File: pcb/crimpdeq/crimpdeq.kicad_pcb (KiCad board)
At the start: 4 copper layers, 30 x 30 mm, 55 parts, among them J10 A-_Cable_Pad, J11 E+_Cable_Pad, J12 E-_Cable_Pad, J2 USB4105-GF-A, J5 B-_Cable_Pad, J6 SW+_Cable_Pad, J7 B+_Cable_Pad, J8 SW-_Cable_Pad, J9 A+_Cable_Pad, Q2 DMG3415U, U1 ESP32-C3-MINI-1, U2 MCP73831T-2ACI/OT, U3 ADS1220, U5 MAX17048G+T10, U6 SY8088

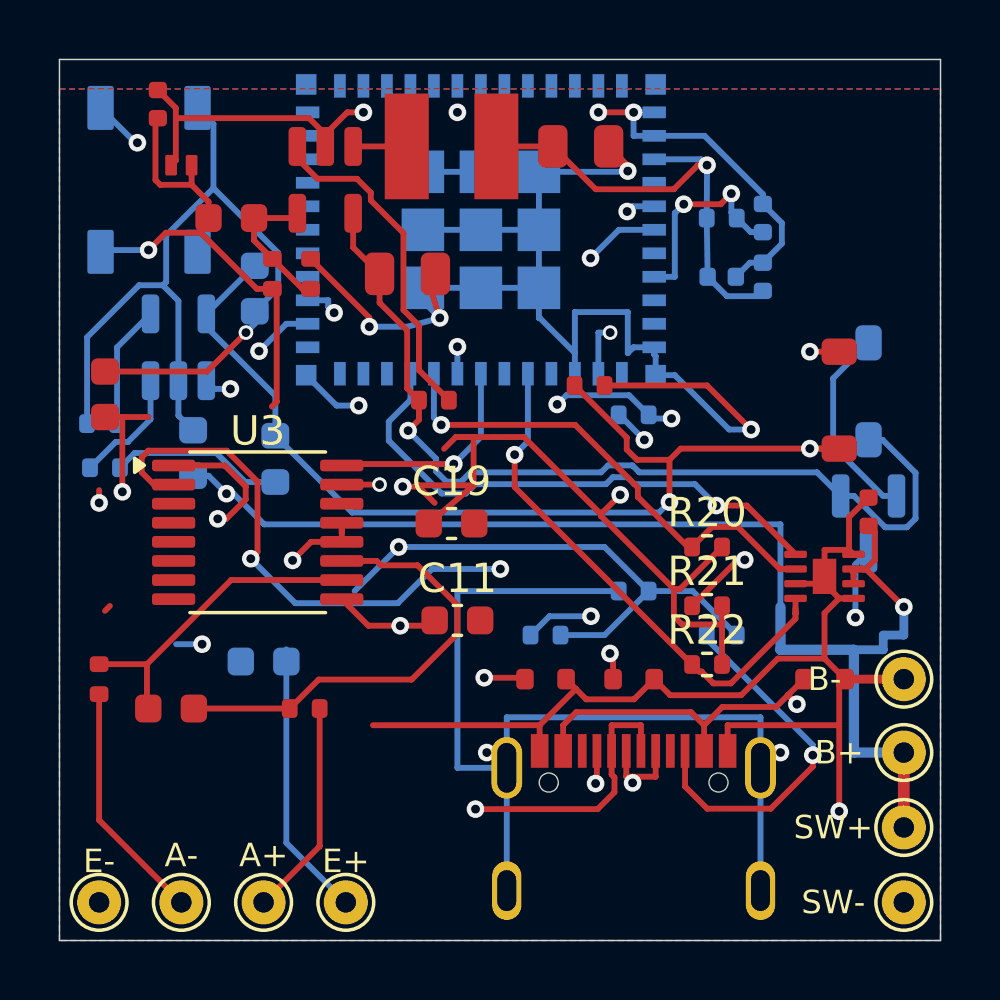
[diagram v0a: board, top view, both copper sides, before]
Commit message: fix: correct SY8088 footprint handedness
Co-authored-by: Cursor <cursoragent@cursor.com>
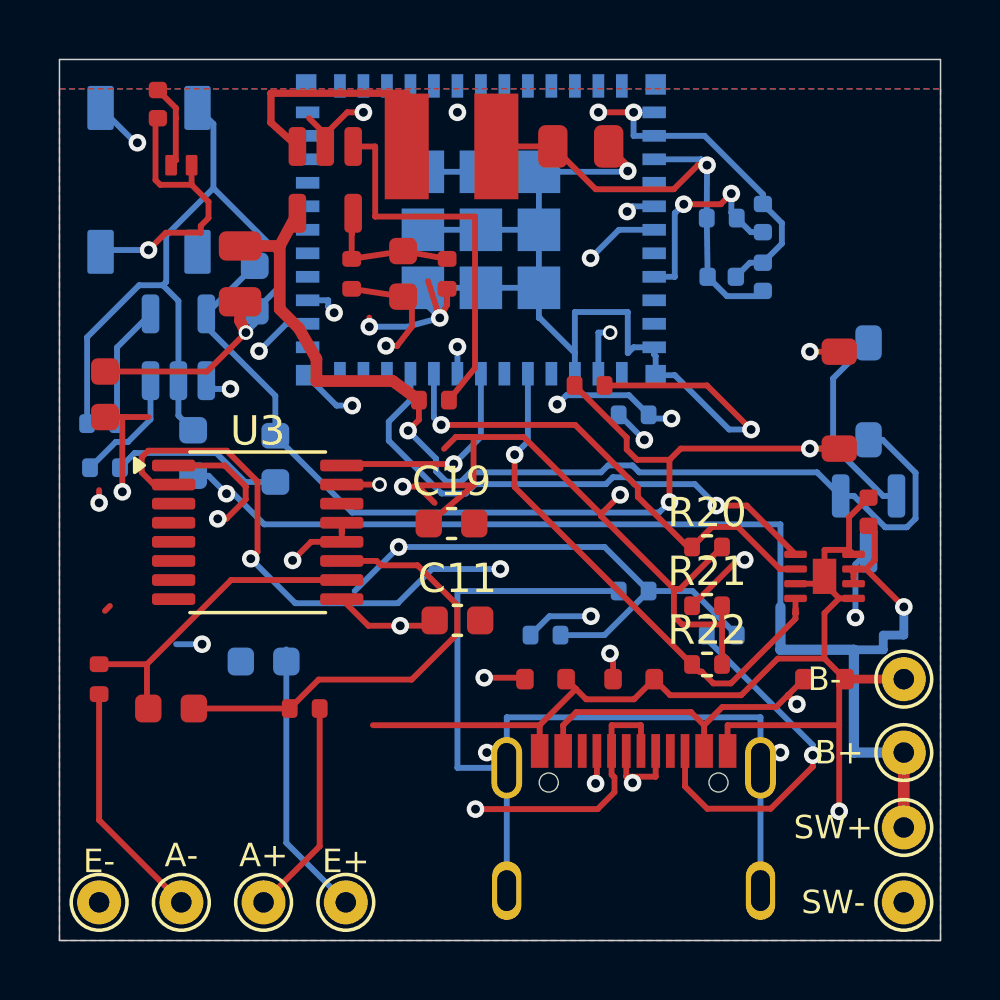
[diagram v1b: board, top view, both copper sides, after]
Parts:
- moved C16 6.15 mm to (139.2, 59.7), turned to 90 degrees
- moved C15 5.70 mm to (133.6, 59.7), turned to -90 degrees
- moved R16 4.65 mm to (140.7, 59.7), turned to -90 degrees
- moved R15 2.70 mm to (137.4, 59.7)
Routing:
- net GND: track 190.4 -> 176.4 mm
- net Buck_Coil: track 1.83 -> 6.84 mm
- net +3V3: track 123.8 -> 127.9 mm, vias 8 -> 9
- net VSYS: track 31.6 -> 35.6 mm
- net ENABLE: track 11.6 -> 13.1 mm

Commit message: fix: correct component footprint handedness
Co-authored-by: Cursor <cursoragent@cursor.com>
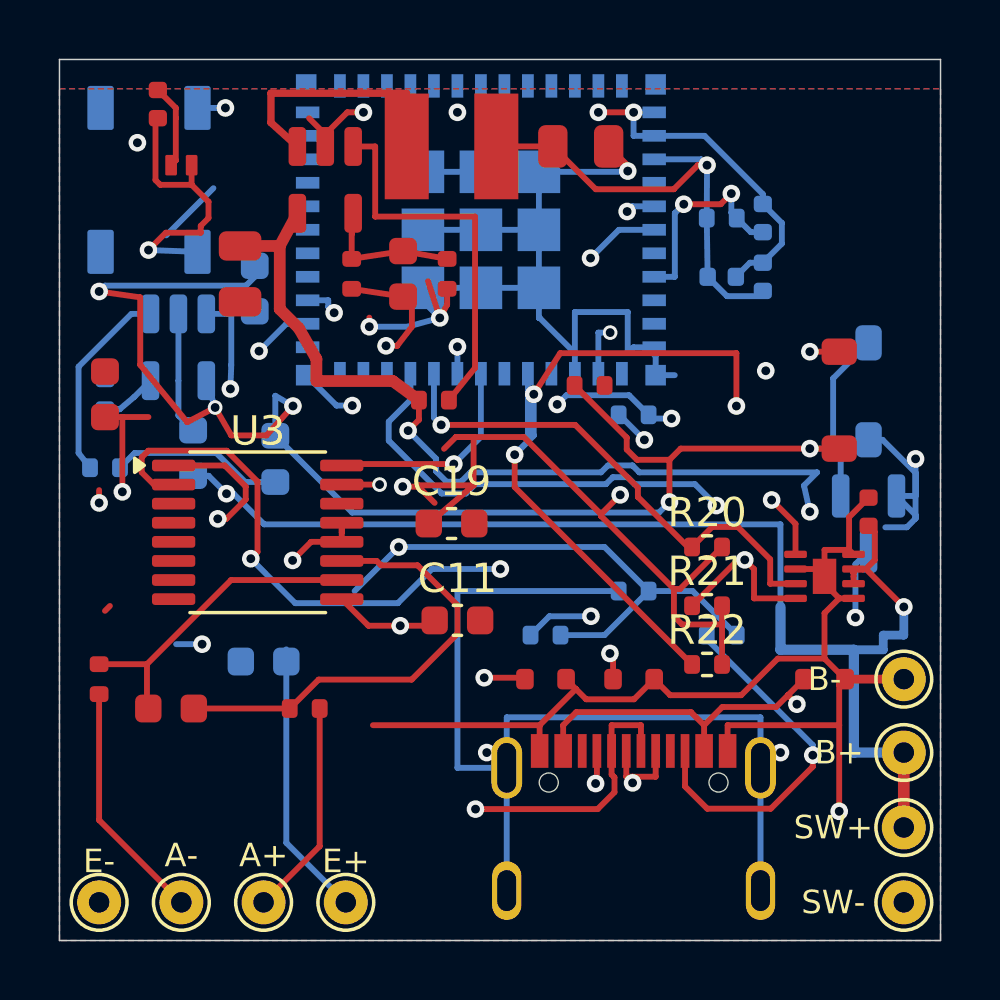
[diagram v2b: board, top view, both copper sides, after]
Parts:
- moved R2 1.00 mm to (129.0, 63.8), turned to -90 degrees
- turned U2 to -90 degrees
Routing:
- net GND: track 176.4 -> 137.9 mm, vias 13 -> 12
- net IO10_ALRT: track 18.2 -> 30.0 mm, vias 1 -> 4
- net VBUS: track 41.7 -> 53.1 mm, vias 2 -> 5
- net VSYS: track 35.6 -> 41.1 mm, vias 1 -> 3
- net Net-(U2-STAT): track 4.06 -> 6.77 mm
- net +BATT: track 47.6 -> 50.2 mm
- net Net-(D4-DIN): track 32.2 -> 34.6 mm, vias 3 -> 4
- net Net-(U2-PROG): track 4.21 -> 1.93 mm
- net IO5_SCK: track 25.5 -> 26.4 mm
- net IO6_SDA: track 16.7 -> 17.4 mm
- net IO7_SCL: track 23.2 -> 22.7 mm

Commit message: fix: align MAX17048 I2C names with TDFN pads
Keep existing copper and GPIO numbers; rename the reversed SDA/SCL
labels and restore missing schematic paths so the board matches the
datasheet pin map.

Co-authored-by: Cursor <cursoragent@cursor.com>
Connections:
- net IO6_SDA renamed IO6_SCL
- net IO7_SCL renamed IO7_SDA
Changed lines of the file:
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@@
 			(layers "F.Cu" "F.Mask" "F.Paste")
 			(roundrect_rratio 0.25)
-			(net "IO7_SCL")
+			(net "IO7_SDA")
 			(pintype "passive")
 		)
@@
 			(layers "F.Cu" "F.Mask" "F.Paste")
 			(roundrect_rratio 0.25)
-			(net "IO6_SDA")
+			(net "IO6_SCL")
 			(pintype "passive")
 		)
@@
 			(layers "F.Cu" "F.Mask" "F.Paste")
 			(roundrect_rratio 0.25)
-			(net "IO6_SDA")
+			(net "IO6_SCL")
 			(pinfunction "SDA_7")
 			(pintype "bidirectional")
@@
 			(layers "F.Cu" "F.Mask" "F.Paste")
 			(roundrect_rratio 0.25)
-			(net "IO7_SCL")
+			(net "IO7_SDA")
 			(pinfunction "SCL_8")
 			(pintype "input")
@@
 			(size 0.4 0.8)
 			(layers "B.Cu" "B.Mask" "B.Paste")
-			(net "IO6_SDA")
+			(net "IO6_SCL")
 			(pinfunction "GPIO6_20")
 			(pintype "bidirectional")
@@
 			(size 0.4 0.8)
 			(layers "B.Cu" "B.Mask" "B.Paste")
-			(net "IO7_SCL")
+			(net "IO7_SDA")
 			(pinfunction "GPIO7_21")
 			(pintype "bidirectional")
@@
 		(width 0.2)
 		(layer "F.Cu")
-		(net "IO7_SCL")
+		(net "IO7_SDA")
 	)
 	(segment
@@
 		(width 0.2)
 		(layer "F.Cu")
-		(net "IO7_SCL")
+		(net "IO7_SDA")
 	)
 	(segment
@@
 		(width 0.2)
 		(layer "F.Cu")
-		(net "IO7_SCL")
+		(net "IO7_SDA")
 	)
 	(segment
@@
 		(width 0.2)
 		(layer "F.Cu")
-		(net "IO7_SCL")
+		(net "IO7_SDA")
 	)
 	(segment
@@
 		(width 0.2)
 		(layer "F.Cu")
-		(net "IO7_SCL")
+		(net "IO7_SDA")
 	)
 	(via
@@
 		(drill 0.3)
 		(layers "F.Cu" "B.Cu")
-		(net "IO7_SCL")
+		(net "IO7_SDA")
 	)
 	(via
@@
 		(drill 0.3)
 		(layers "F.Cu" "B.Cu")
-		(net "IO7_SCL")
+		(net "IO7_SDA")
 	)
 	(segment
@@
 		(width 0.2)
 		(layer "B.Cu")
-		(net "IO7_SCL")
+		(net "IO7_SDA")
 	)
 	(segment
@@
 		(width 0.2)
 		(layer "B.Cu")
-		(net "IO7_SCL")
+		(net "IO7_SDA")
 	)
 	(segment
@@
 		(width 0.2)
 		(layer "B.Cu")
-		(net "IO7_SCL")
+		(net "IO7_SDA")
 	)
 	(segment
@@
 		(width 0.2)
 		(layer "B.Cu")
-		(net "IO7_SCL")
+		(net "IO7_SDA")
 	)
 	(segment
@@
 		(width 0.2)
 		(layer "B.Cu")
-		(net "IO7_SCL")
+		(net "IO7_SDA")
 	)
 	(segment
@@
 		(width 0.2)
 		(layer "B.Cu")
-		(net "IO7_SCL")
+		(net "IO7_SDA")
 	)
 	(segment
@@
 		(width 0.2)
 		(layer "B.Cu")
-		(net "IO7_SCL")
+		(net "IO7_SDA")
 	)
 	(segment
@@
 		(width 0.2)
 		(layer "B.Cu")
-		(net "IO7_SCL")
+		(net "IO7_SDA")
 	)
 	(segment
@@
 		(width 0.2)
 		(layer "B.Cu")
-		(net "IO7_SCL")
+		(net "IO7_SDA")
 	)
 	(segment
@@
 		(width 0.2)
 		(layer "B.Cu")
-		(net "IO7_SCL")
+		(net "IO7_SDA")
 	)
 	(segment
@@
 		(width 0.2)
 		(layer "B.Cu")
-		(net "IO7_SCL")
+		(net "IO7_SDA")
 	)
 	(segment
@@
 		(width 0.2)
 		(layer "B.Cu")
-		(net "IO7_SCL")
+		(net "IO7_SDA")
 	)
 	(segment
@@
 		(width 0.2)
 		(layer "In2.Cu")
-		(net "IO7_SCL")
+		(net "IO7_SDA")
 	)
 	(segment
@@
 		(width 0.2)
 		(layer "In2.Cu")
-		(net "IO7_SCL")
+		(net "IO7_SDA")
 	)
 	(via
@@
 		(width 0.2)
 		(layer "F.Cu")
-		(net "IO6_SDA")
+		(net "IO6_SCL")
 	)
 	(segment
@@
 		(width 0.2)
 		(layer "F.Cu")
-		(net "IO6_SDA")
+		(net "IO6_SCL")
 	)
 	(segment
@@
 		(width 0.2)
 		(layer "F.Cu")
-		(net "IO6_SDA")
+		(net "IO6_SCL")
 	)
 	(segment
@@
 		(width 0.2)
 		(layer "F.Cu")
-		(net "IO6_SDA")
+		(net "IO6_SCL")
 	)
 	(segment
@@
 		(width 0.2)
 		(layer "F.Cu")
-		(net "IO6_SDA")
+		(net "IO6_SCL")
 	)
 	(segment
@@
 		(width 0.2)
 		(layer "F.Cu")
-		(net "IO6_SDA")
+		(net "IO6_SCL")
 	)
 	(segment
@@
 		(width 0.2)
 		(layer "F.Cu")
-		(net "IO6_SDA")
+		(net "IO6_SCL")
 	)
 	(segment
@@
 		(width 0.2)
 		(layer "F.Cu")
-		(net "IO6_SDA")
+		(net "IO6_SCL")
 	)
 	(segment
@@
 		(width 0.2)
 		(layer "F.Cu")
-		(net "IO6_SDA")
+		(net "IO6_SCL")
 	)
 	(segment
@@
 		(width 0.2)
 		(layer "F.Cu")
-		(net "IO6_SDA")
+		(net "IO6_SCL")
 	)
 	(via
@@
 		(drill 0.3)
 		(layers "F.Cu" "B.Cu")
-		(net "IO6_SDA")
+		(net "IO6_SCL")
 	)
 	(segment
@@
 		(width 0.2)
 		(layer "B.Cu")
-		(net "IO6_SDA")
+		(net "IO6_SCL")
 	)
 	(segment
@@
 		(width 0.2)
 		(layer "B.Cu")
-		(net "IO6_SDA")
+		(net "IO6_SCL")
 	)
 	(segment

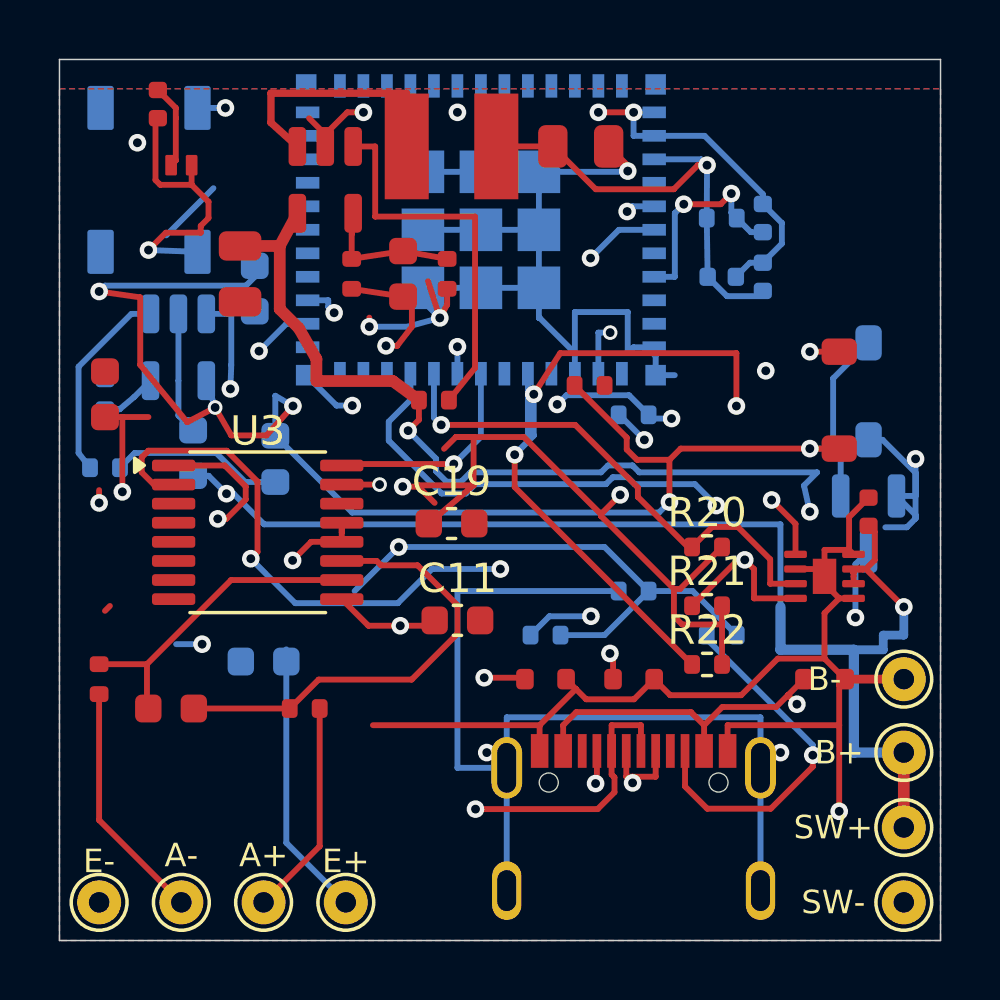
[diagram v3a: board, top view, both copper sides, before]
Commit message: fix: cluster analog filter and length-match USB pair
Shorten and symmetrize AIN0/AIN1 over the RC cluster, and rematch USB D+/D− so the pair is DRC-clean at full-speed lengths.

Co-authored-by: Cursor <cursoragent@cursor.com>
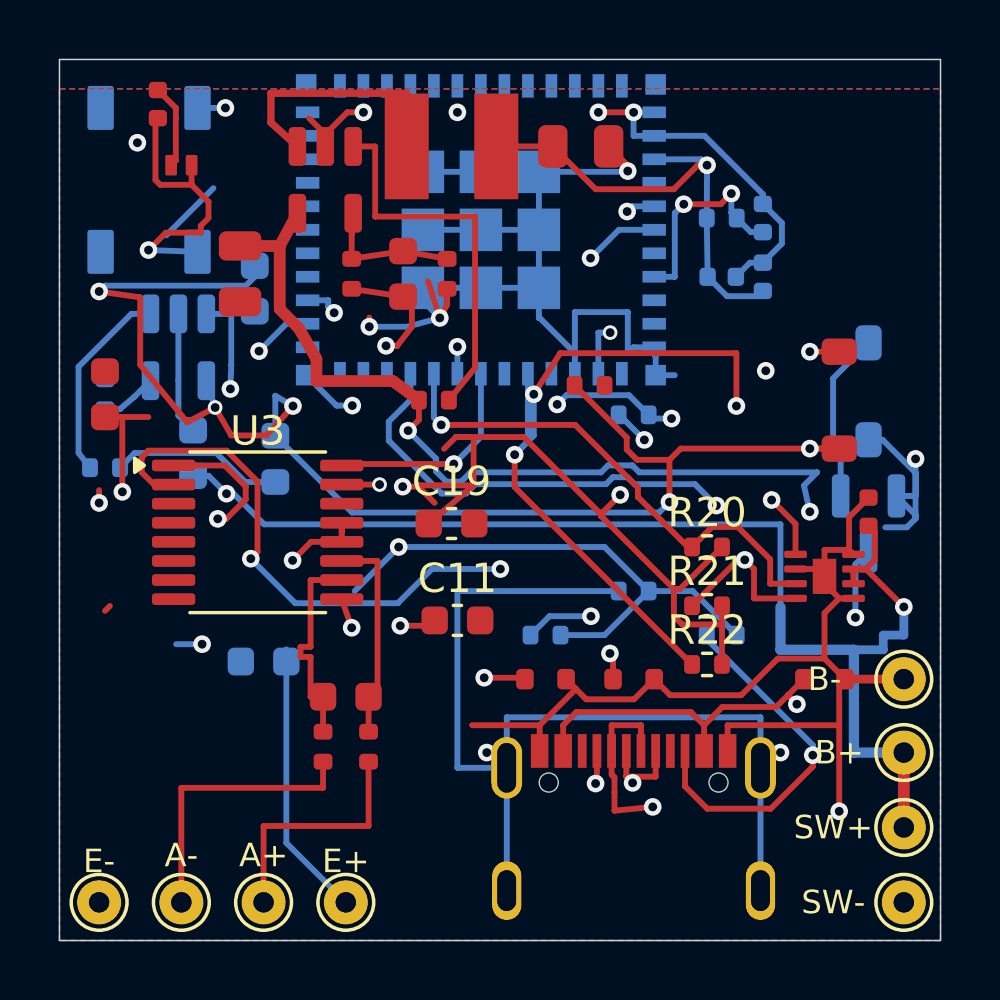
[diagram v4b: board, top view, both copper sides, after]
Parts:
- moved R8 7.96 mm to (136.4, 75.8)
- moved C12 5.96 mm to (137.2, 74.1)
- moved R7 2.53 mm to (138.0, 75.8), turned to -90 degrees
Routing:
- net USB_D+: track 28.8 -> 41.5 mm
- net USB_D-: track 31.7 -> 41.5 mm
- net Net-(U3-AIN0): track 15.6 -> 7.34 mm
- net Net-(U3-AIN1): track 11.0 -> 7.34 mm
- net GND: track 137.9 -> 134.6 mm
- net A-: track 8.25 -> 9.62 mm
- net +3V3: track 127.9 -> 126.6 mm, vias 9 -> 10
- net A+: track 7.39 -> 8.36 mm
